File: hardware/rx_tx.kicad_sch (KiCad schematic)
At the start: 14 parts, among them J4 SMA_Conn, U4 MIC5317-3.0YD5-TR, U5 MAX41462GUB+, Y1 ECS-160-12-37B-CTN-TR

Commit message: Updated schematic, PCB and fabrication files
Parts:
- added C9: 100p, Capacitor_SMD:C_0603_1608Metric, symbol Device:C
- added L4: MI0805K400R-10, Inductor_SMD:L_0805_2012Metric, symbol Device:L
- renumbered C6 to C10, C7 to C11, C8 to C12, C9 to C13, C10 to C14, C5 to C8, L2 to L5, L3 to L6
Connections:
- net +5V: now also L4.1; no longer C8.2, U4.1 (VIN), U4.3 (EN)
- net GND: now also C9.2
- new net 5VLDOIn: C8.2, C9.1, L4.2, U4.1 (VIN), U4.3 (EN)
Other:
- moved on the sheet: C8

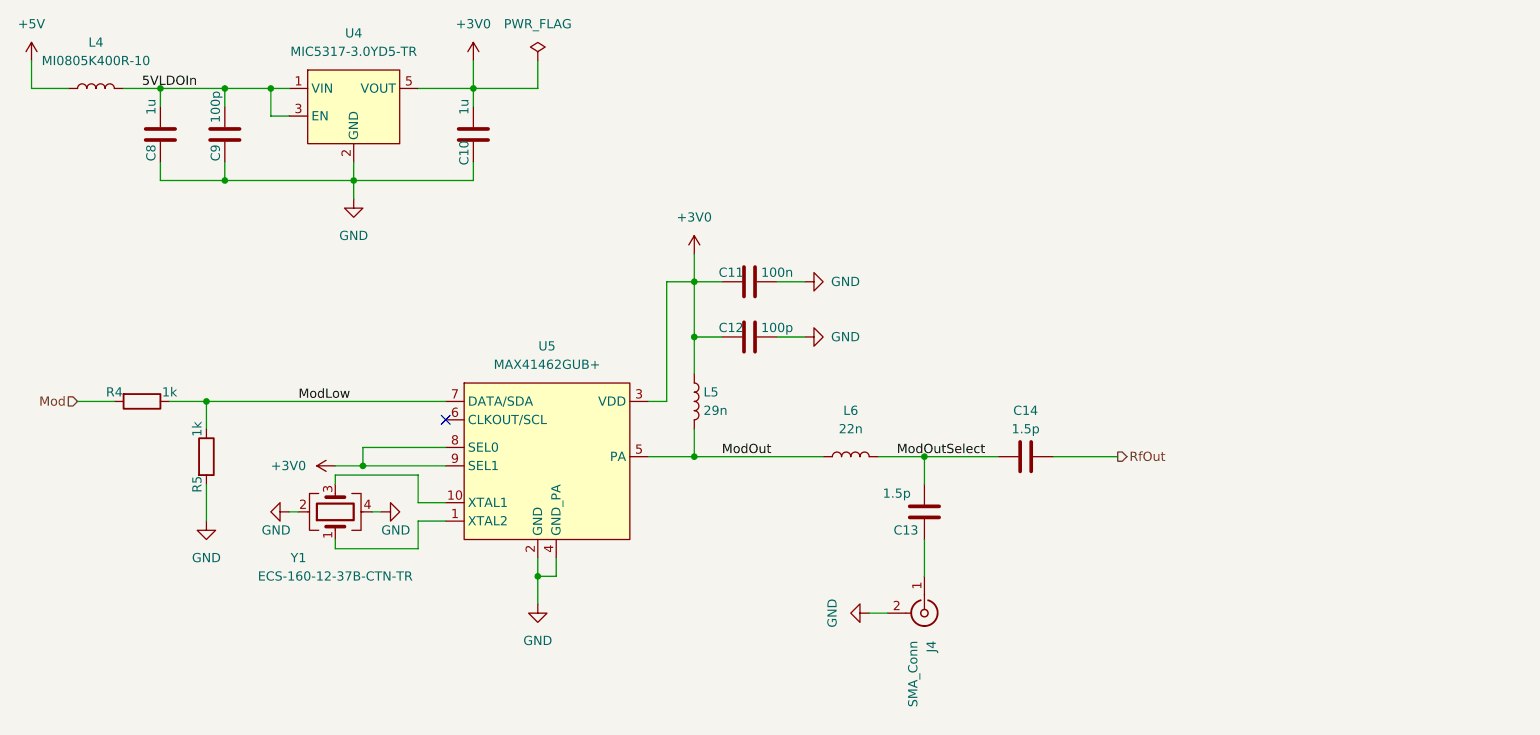
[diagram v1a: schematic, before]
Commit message: Rev 2. Using USB-C, configurable Tx, op-amp based LF amplifier, tri-color indicator. Using platformIO for firmware, splitted code into separate files.
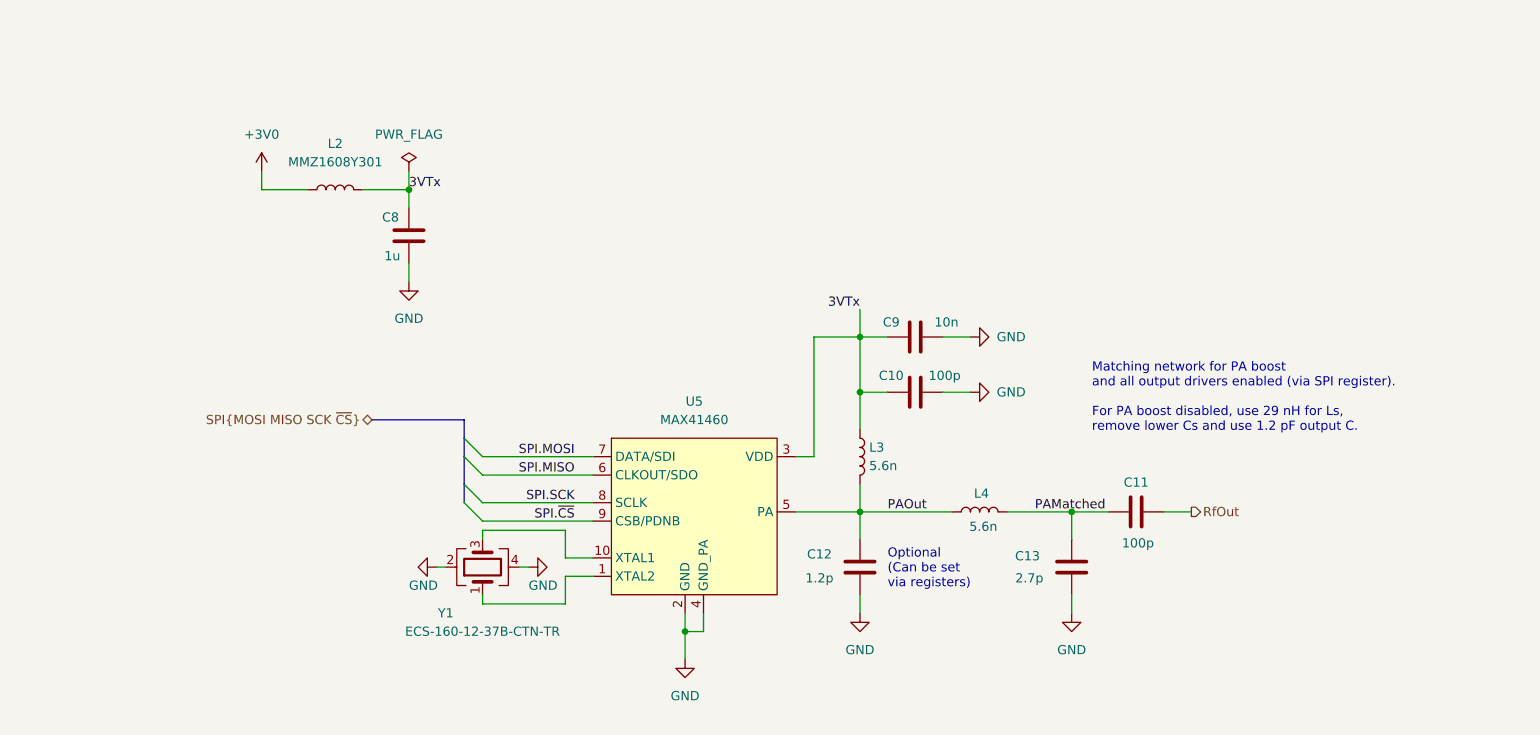
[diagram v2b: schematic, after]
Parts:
- removed C10: 1u, Capacitor_SMD:C_0603_1608Metric, symbol Device:C
- removed C9: 100p, Capacitor_SMD:C_0603_1608Metric, symbol Device:C
- removed J4: SMA_Conn, Connector_Coaxial:SMA_Samtec_SMA-J-P-X-ST-EM1_EdgeMount, symbol Connector:Conn_Coaxial
- removed L4: MI0805K400R-10, Inductor_SMD:L_0805_2012Metric, symbol Device:L
- removed R4, R5: 1k, Resistor_SMD:R_0603_1608Metric, symbol Device:R
- removed U4: MIC5317-3.0YD5-TR, Package_TO_SOT_SMD:SOT-23-5, symbol ProjLib:MIC5317
- added C12: 1.2p, Capacitor_SMD:C_0603_1608Metric, symbol Device:C
- added L2: MMZ1608Y301, Inductor_SMD:L_0603_1608Metric, symbol Device:L
- C11: renamed from C14; value 1.5p -> 100p
- C13: value 1.5p -> 2.7p; now in the parts list
- C9: renamed from C11; value 100n -> 10n
- L3: renamed from L5; value 29n -> 5.6n
- L4: renamed from L6; value 22n -> 5.6n
- U5: value MAX41462GUB+ -> MAX41460; footprint ProjLib:uMax-10 -> Package_SO:VSSOP-10_3x3mm_P0.5mm; symbol ProjLib:MAX41462 -> ProjLib:MAX41460
- Y1: footprint ProjLib:Crystal_SMD_2x1.6mm -> Crystal:Crystal_SMD_2016-4Pin_2.0x1.6mm
- renumbered C12 to C10
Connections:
- net +3V0: now also L2.1; no longer C10.2, C9.1, L3.1, U5.3 (VDD), U5.8 (SEL0), U5.9 (SEL1)
- net GND: now also C13.2, C12.2
- net SPI.MISO: now reaches U5.6 (CLKOUT/SDO)
- net 5VLDOIn renamed 3VTx
- net 3VTx: now also C10.2, C9.1, L3.1, U5.3 (VDD), L2.2
- net ModLow renamed SPI.MOSI
- net ModOut renamed PAOut
- net PAOut: now also C12.1
- net ModOutSelect renamed PAMatched
- new net SPI.SCK: U5.8 (SCLK)
- new net SPI.~{CS}: U5.9 (CSB/PDNB)
- no-connect marks 1 -> 0
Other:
- note added: "Matching network for PA boost and all output drivers enabled (via SPI register). For PA boost disabled, use 29 nH for Ls, remove lower Cs and use 1.2 pF output C."
- note added: "Optional (Can be set via registers)"
- moved on the sheet: C10, C11, C9, L3, L4, U5, Y1

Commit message: Rev 3. Back to transistor-based design since op-amp approach did not work well. Using UART bridge from other brand as FTDI was sold out.
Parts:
- removed C8: 1u, Capacitor_SMD:C_0603_1608Metric, symbol Device:C
- removed L2: MMZ1608Y301, Inductor_SMD:L_0603_1608Metric, symbol Device:L
- C10: renamed from C12; now not fitted; now left out of the parts list
- renumbered C13 to C11, C9 to C7, C10 to C8, C11 to C9, L3 to L1, L4 to L2
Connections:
- net 3VTx is gone; now on net +3V0: C7.1, C8.2, L1.1, U5.3 (VDD)

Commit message: Rev 4. Removed coupler and detector IC. Using simple diode as detector.
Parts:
- renumbered C11 to C10, C7 to C6, C8 to C7, C9 to C8, C10 to C9, U5 to U4
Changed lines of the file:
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@@
 		(dnp no)
 		(fields_autoplaced yes)
-		(property "Reference" "#PWR022"
+		(property "Reference" "#PWR020"
 			(at 146.05 68.58 0)
 			(effects
@@
 			(project "DetectorReader"
 				(path "/e63e39d7-6ac0-4ffd-8aa3-1841a4541b55/33805b45-ff14-4118-a0cb-7978d211ce11"
-					(reference "#PWR022")
+					(reference "#PWR020")
 					(unit 1)
 				)
@@
 		(on_board yes)
 		(dnp no)
-		(property "Reference" "C8"
+		(property "Reference" "C7"
 			(at 150.368 75.184 90)
 			(effects
@@
 			(project ""
 				(path "/e63e39d7-6ac0-4ffd-8aa3-1841a4541b55/33805b45-ff14-4118-a0cb-7978d211ce11"
-					(reference "C8")
+					(reference "C7")
 					(unit 1)
 				)
@@
 		(dnp no)
 		(fields_autoplaced yes)
-		(property "Reference" "#PWR028"
+		(property "Reference" "#PWR026"
 			(at 175.26 114.3 0)
 			(effects
@@
 			(project "DetectorReader"
 				(path "/e63e39d7-6ac0-4ffd-8aa3-1841a4541b55/33805b45-ff14-4118-a0cb-7978d211ce11"
-					(reference "#PWR028")
+					(reference "#PWR026")
 					(unit 1)
 				)
@@
 		(on_board yes)
 		(dnp no)
-		(property "Reference" "C9"
+		(property "Reference" "C8"
 			(at 184.15 89.916 90)
 			(effects
@@
 			(project ""
 				(path "/e63e39d7-6ac0-4ffd-8aa3-1841a4541b55/33805b45-ff14-4118-a0cb-7978d211ce11"
-					(reference "C9")
+					(reference "C8")
 					(unit 1)
 				)
@@
 		(dnp no)
 		(fields_autoplaced yes)
-		(property "Reference" "U5"
+		(property "Reference" "U4"
 			(at 123.19 78.74 0)
 			(effects
@@
 			(project ""
 				(path "/e63e39d7-6ac0-4ffd-8aa3-1841a4541b55/33805b45-ff14-4118-a0cb-7978d211ce11"
-					(reference "U5")
+					(reference "U4")
 					(unit 1)
 				)
@@
 		(on_board yes)
 		(dnp no)
-		(property "Reference" "#PWR024"
+		(property "Reference" "#PWR022"
 			(at 167.64 77.47 0)
 			(effects
@@
 			(project ""
 				(path "/e63e39d7-6ac0-4ffd-8aa3-1841a4541b55/33805b45-ff14-4118-a0cb-7978d211ce11"
-					(reference "#PWR024")
+					(reference "#PWR022")
 					(unit 1)
 				)
@@
 		(on_board yes)
 		(dnp no)
-		(property "Reference" "#PWR025"
+		(property "Reference" "#PWR023"
 			(at 81.28 101.6 0)
 			(effects
@@
 			(project ""
 				(path "/e63e39d7-6ac0-4ffd-8aa3-1841a4541b55/33805b45-ff14-4118-a0cb-7978d211ce11"
-					(reference "#PWR025")
+					(reference "#PWR023")
 					(unit 1)
 				)
@@
 		(dnp no)
 		(fields_autoplaced yes)
-		(property "Reference" "#PWR029"
+		(property "Reference" "#PWR027"
 			(at 121.92 120.65 0)
 			(effects
@@
 			(project ""
 				(path "/e63e39d7-6ac0-4ffd-8aa3-1841a4541b55/33805b45-ff14-4118-a0cb-7978d211ce11"
-					(reference "#PWR029")
+					(reference "#PWR027")
 					(unit 1)
 				)
@@
 		(on_board yes)
 		(dnp yes)
-		(property "Reference" "C10"
+		(property "Reference" "C9"
 			(at 140.462 99.822 0)
 			(effects
@@
 			(project "DetectorReader"
 				(path "/e63e39d7-6ac0-4ffd-8aa3-1841a4541b55/33805b45-ff14-4118-a0cb-7978d211ce11"
-					(reference "C10")
+					(reference "C9")
 					(unit 1)
 				)
@@
 		(on_board yes)
 		(dnp no)
-		(property "Reference" "#PWR026"
+		(property "Reference" "#PWR024"
 			(at 106.68 101.6 0)
 			(effects
@@
 			(project ""
 				(path "/e63e39d7-6ac0-4ffd-8aa3-1841a4541b55/33805b45-ff14-4118-a0cb-7978d211ce11"
-					(reference "#PWR026")
+					(reference "#PWR024")
 					(unit 1)
 				)
@@
 		(on_board yes)
 		(dnp no)
-		(property "Reference" "#PWR023"
+		(property "Reference" "#PWR021"
 			(at 167.64 69.85 0)
 			(effects
@@
 			(project ""
 				(path "/e63e39d7-6ac0-4ffd-8aa3-1841a4541b55/33805b45-ff14-4118-a0cb-7978d211ce11"
-					(reference "#PWR023")
+					(reference "#PWR021")
 					(unit 1)
 				)
@@
 		(on_board yes)
 		(dnp no)
-		(property "Reference" "C7"
+		(property "Reference" "C6"
 			(at 150.368 67.818 90)
 			(effects
@@
 			(project ""
 				(path "/e63e39d7-6ac0-4ffd-8aa3-1841a4541b55/33805b45-ff14-4118-a0cb-7978d211ce11"
-					(reference "C7")
+					(reference "C6")
 					(unit 1)
 				)
@@
 		(on_board yes)
 		(dnp no)
-		(property "Reference" "C11"
+		(property "Reference" "C10"
 			(at 169.164 100.076 0)
 			(effects
@@
 			(project "DetectorReader"
 				(path "/e63e39d7-6ac0-4ffd-8aa3-1841a4541b55/33805b45-ff14-4118-a0cb-7978d211ce11"
-					(reference "C11")
+					(reference "C10")
 					(unit 1)
 				)
@@
 		(dnp no)
 		(fields_autoplaced yes)
-		(property "Reference" "#PWR027"
+		(property "Reference" "#PWR025"
 			(at 146.05 114.3 0)
 			(effects
@@
 			(project "DetectorReader"
 				(path "/e63e39d7-6ac0-4ffd-8aa3-1841a4541b55/33805b45-ff14-4118-a0cb-7978d211ce11"
-					(reference "#PWR027")
-					(unit 1)
-				)
+					(reference "#PWR025")
+					(unit 1)
+				)
